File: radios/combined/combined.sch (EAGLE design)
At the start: 17 parts

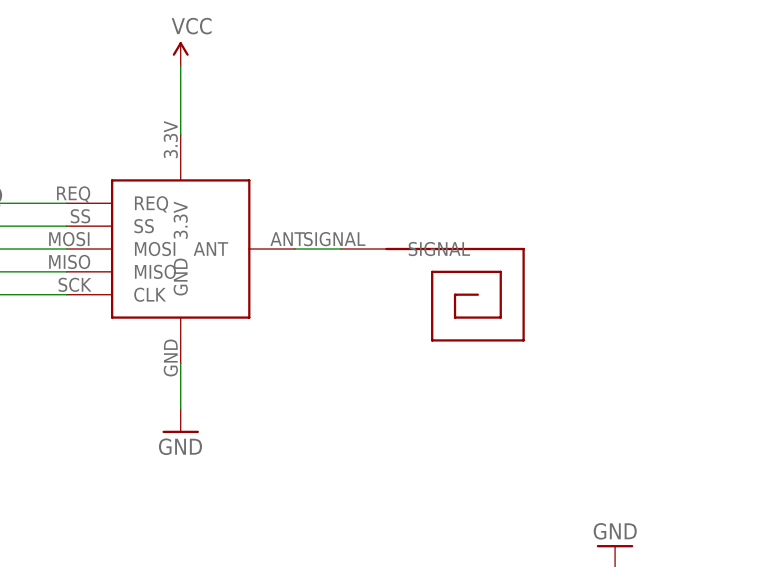
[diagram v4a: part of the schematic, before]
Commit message: replaced chip antenna with pad for wire
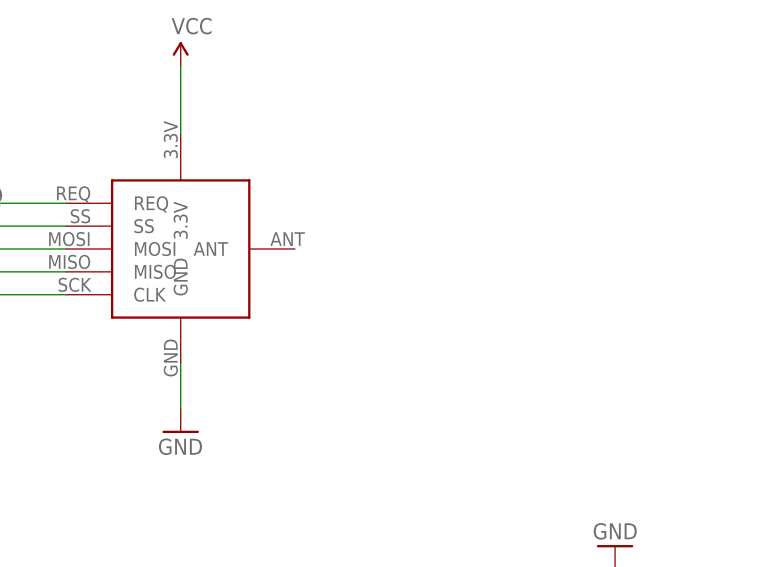
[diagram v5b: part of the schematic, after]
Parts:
- removed U$2: 915MHZ-ANTENNA-SMD, ITP_Lab:915MHZ-ANTENNA-SMD
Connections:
- removed net N$6: U$1.ANT, U$2.SIGNAL
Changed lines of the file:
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@@
 <part name="GND1" library="SparkFun" deviceset="GND" device=""/>
 <part name="P+1" library="SparkFun" deviceset="3.3V" device="" value="VCC"/>
-<part name="U$2" library="ITP_Lab" deviceset="915MHZ-ANTENNA-SMD" device=""/>
 <part name="C3" library="SparkFun-Capacitors" deviceset="CAP_POL" device="1206" value="10uF"/>
 <part name="GND5" library="SparkFun" deviceset="GND" device=""/>
@@
 <instance part="GND1" gate="1" x="195.58" y="187.96"/>
 <instance part="P+1" gate="G$1" x="195.58" y="228.6"/>
-<instance part="U$2" gate="G$1" x="218.44" y="208.28" rot="R270"/>
 <instance part="C3" gate="G$1" x="106.68" y="210.82" rot="R180"/>
 <instance part="GND5" gate="1" x="106.68" y="220.98" rot="R180"/>
@@
 </segment>
 </net>
-<net name="N$6" class="0">
-<segment>
-<pinref part="U$1" gate="G$1" pin="ANT"/>
-<pinref part="U$2" gate="G$1" pin="SIGNAL"/>
-<wire x1="213.36" y1="208.28" x2="208.28" y2="208.28" width="0.1524" layer="91"/>
-</segment>
-</net>
